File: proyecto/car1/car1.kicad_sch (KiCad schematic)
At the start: 26 parts, among them J1 HC-sr04, J10 vcc Edu ciaa, J11 Adafruit A, J12 Adafruit B, J2 HC-sr04, J3 HC-sr04, J4 usb c socket, J5 SERVO, J6 Conn_01x08_Socket, J7 Conn_01x08_Socket, J8 Conn_01x19, J9 Conn_01x19

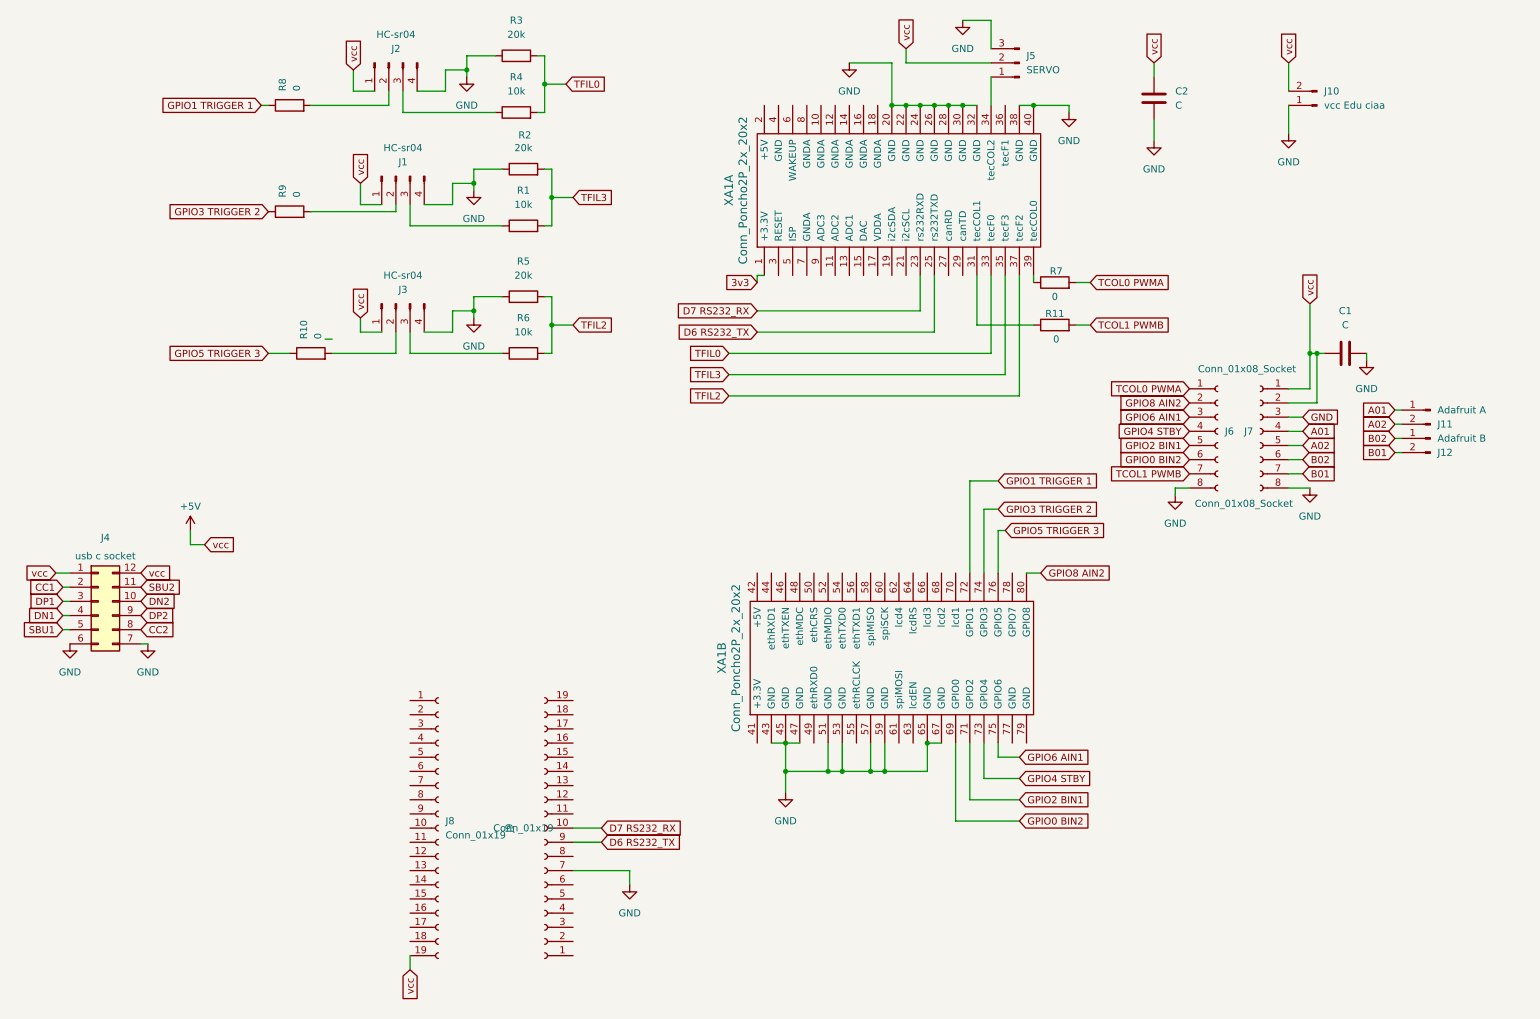
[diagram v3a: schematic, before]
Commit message: cambio de pines
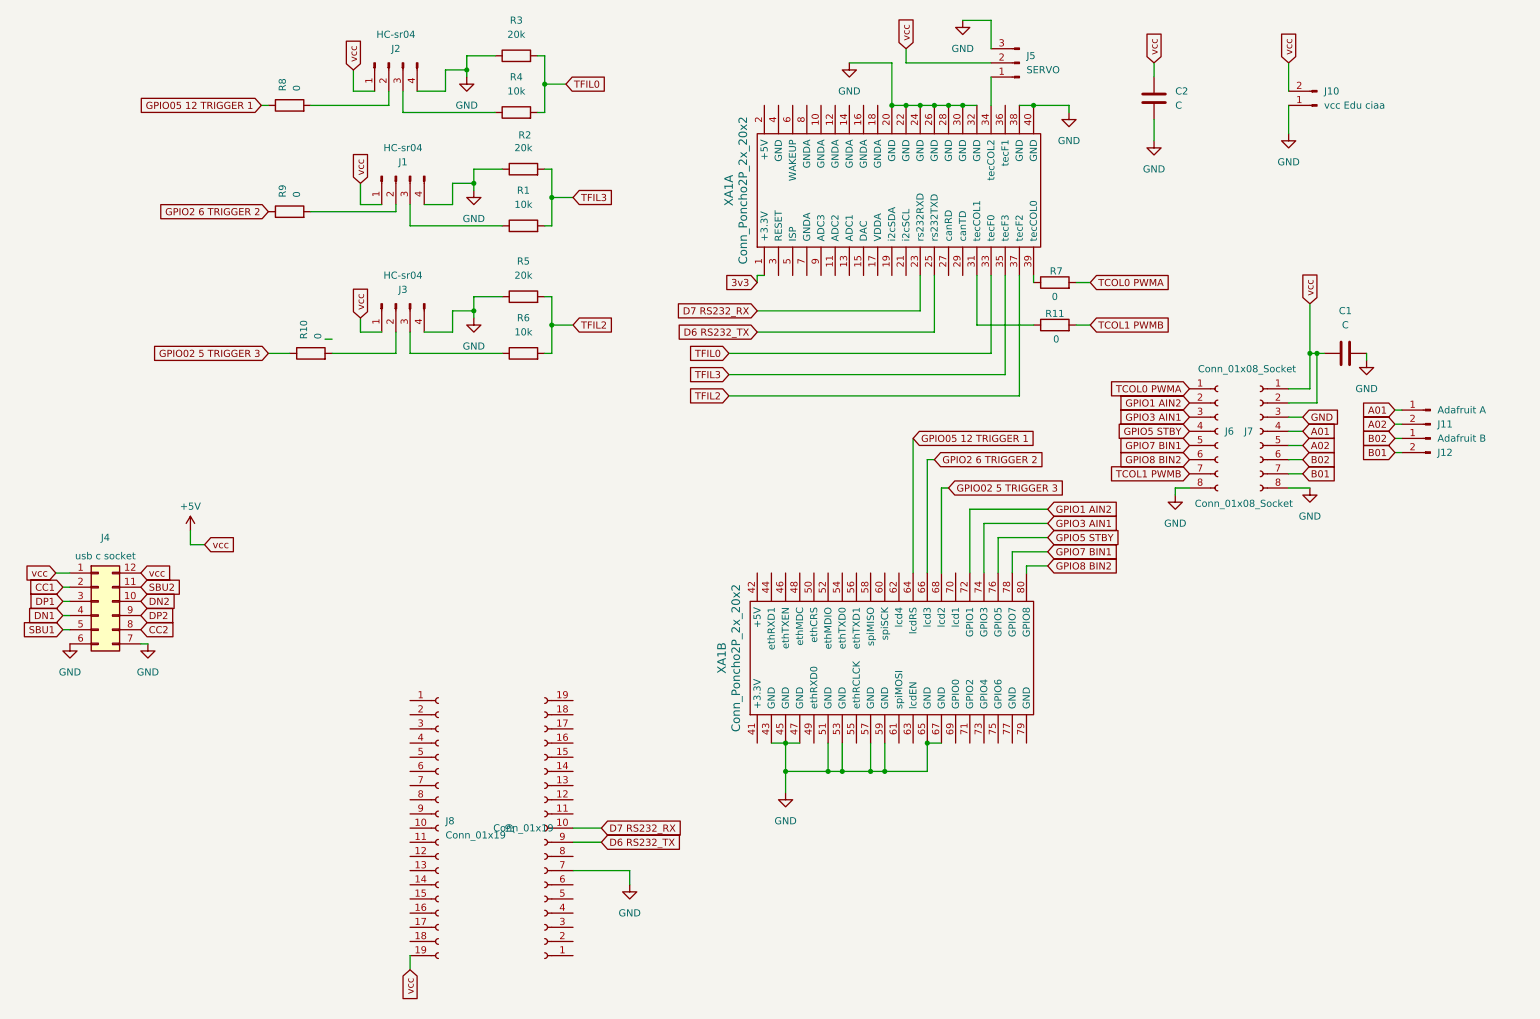
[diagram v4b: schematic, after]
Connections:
- net GPIO05 12 TRIGGER 1: now reaches XA1.64 (lcdRS)
- net GPIO05 12 TRIGGER 1: now also R8.1
- net GPIO2 6  TRIGGER 2: now reaches XA1.66 (lcd3)
- net GPIO2 6  TRIGGER 2: now also R9.1
- net GPIO02 5 TRIGGER 3: now reaches XA1.68 (lcd2)
- net GPIO02 5 TRIGGER 3: now also R10.1
- net GPIO7 BIN1: now reaches XA1.78 (GPIO7)
- net GPIO7 BIN1: now also J6.5 (Pin_5)
- net GPIO0 BIN2: no longer names the net of XA1.69 (GPIO0)
- net GPIO0 BIN2: no longer J6.6 (Pin_6)
- net GPIO1 TRIGGER 1 renamed GPIO1 AIN2
- net GPIO1 AIN2: now also J6.2 (Pin_2); no longer R8.1
- net GPIO2 BIN1: no longer names the net of XA1.71 (GPIO2)
- net GPIO2 BIN1: no longer J6.5 (Pin_5)
- net GPIO3  TRIGGER 2 renamed GPIO3 AIN1
- net GPIO3 AIN1: now also J6.3 (Pin_3); no longer R9.1
- net GPIO4 STBY: no longer names the net of XA1.73 (GPIO4)
- net GPIO4 STBY: no longer J6.4 (Pin_4)
- net GPIO5 TRIGGER 3 renamed GPIO5 STBY
- net GPIO5 STBY: now also J6.4 (Pin_4); no longer R10.1
- net GPIO6 AIN1: no longer names the net of XA1.75 (GPIO6)
- net GPIO6 AIN1: no longer J6.3 (Pin_3)
- net GPIO8 AIN2 renamed GPIO8 BIN2
- net GPIO8 BIN2: now also J6.6 (Pin_6); no longer J6.2 (Pin_2)

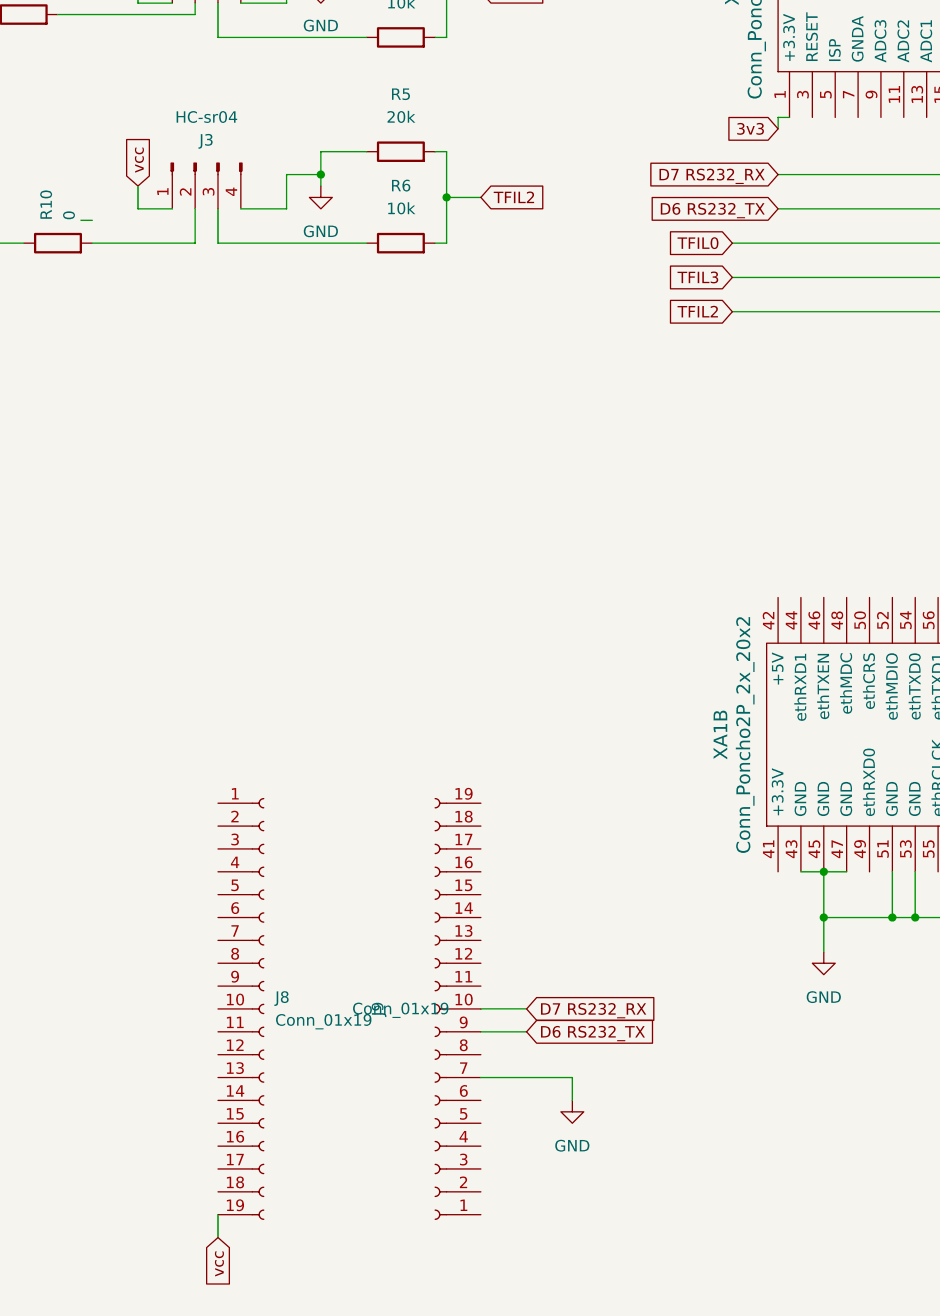
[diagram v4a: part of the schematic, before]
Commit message: fix esp32
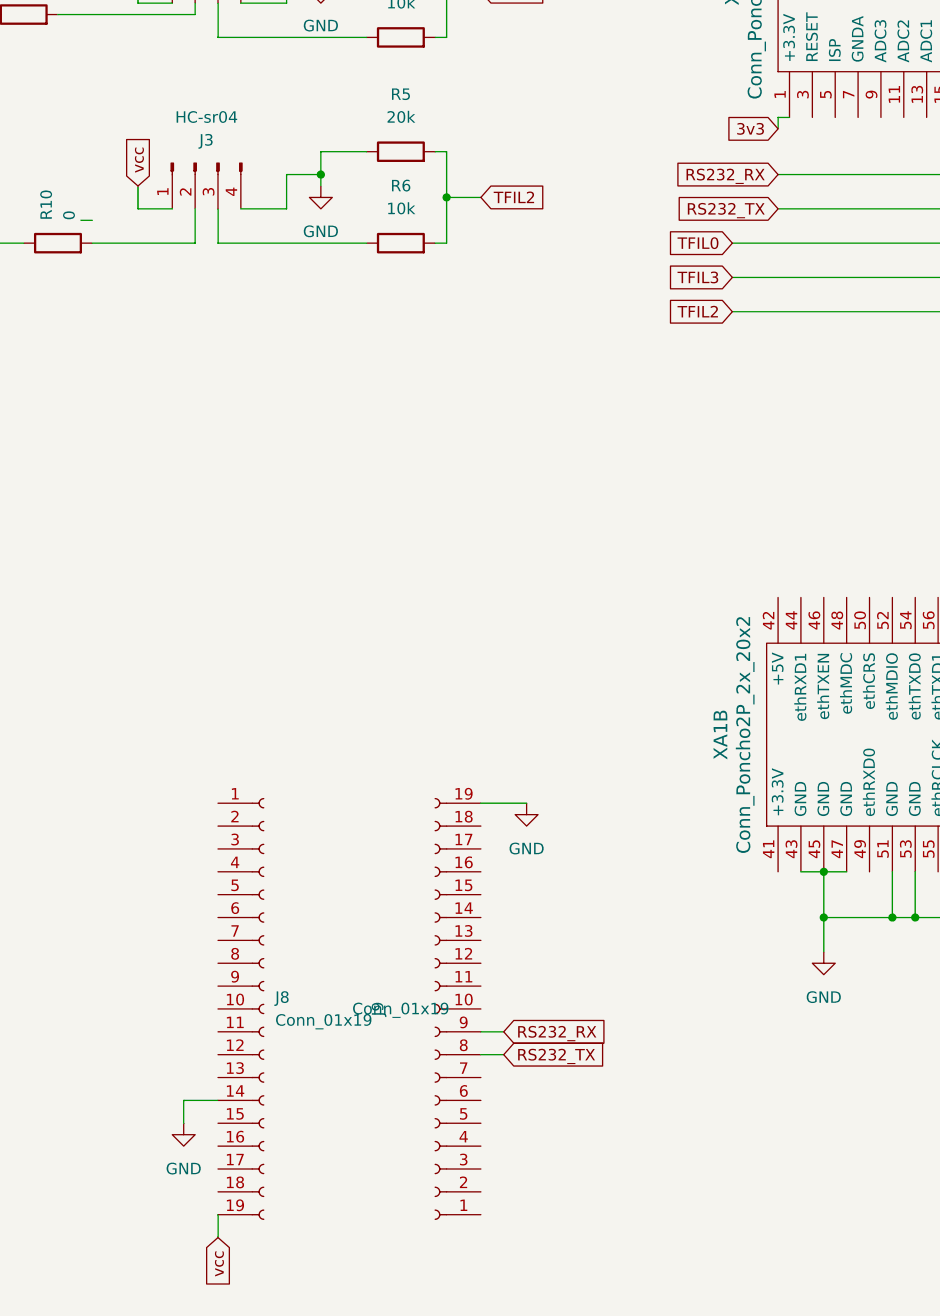
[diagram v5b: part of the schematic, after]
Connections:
- net GND: now also J8.14 (Pin_14), J9.19 (Pin_19); no longer J9.7 (Pin_7)
- net RS232_TX: now reaches J9.8 (Pin_8)
- net RS232_TX: now also XA1.25 (rs232TXD)
- net D6  RS232_TX renamed RS232_RX
- net RS232_RX: now also XA1.23 (rs232RXD); no longer XA1.25 (rs232TXD)
- net D7  RS232_RX: no longer names the net of J9.10 (Pin_10)
- net D7  RS232_RX: no longer XA1.23 (rs232RXD)
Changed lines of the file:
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@@
 	(wire
 		(pts
-			(xy 129.54 167.64) (xy 129.54 170.18)
-		)
-		(stroke
-			(width 0)
-			(type default)
-		)
-	)
-	(wire
-		(pts
 			(xy 254 74.93) (xy 252.73 74.93)
 		)
@@
 	(wire
 		(pts
-			(xy 119.38 167.64) (xy 129.54 167.64)
-		)
-		(stroke
-			(width 0)
-			(type default)
-		)
-	)
-	(wire
-		(pts
 			(xy 247.65 30.48) (xy 247.65 35.56)
 		)
@@
 	(wire
 		(pts
-			(xy 124.46 162.56) (xy 119.38 162.56)
+			(xy 27.94 124.46) (xy 29.21 124.46)
 		)
 		(stroke
@@
 	(wire
 		(pts
-			(xy 27.94 124.46) (xy 29.21 124.46)
+			(xy 119.38 162.56) (xy 121.92 162.56)
 		)
 		(stroke
@@
 	(wire
 		(pts
+			(xy 119.38 165.1) (xy 121.92 165.1)
+		)
+		(stroke
+			(width 0)
+			(type default)
+		)
+	)
+	(wire
+		(pts
 			(xy 86.36 30.48) (xy 86.36 27.94)
 		)
@@
 	(wire
 		(pts
+			(xy 86.36 170.18) (xy 86.36 172.72)
+		)
+		(stroke
+			(width 0)
+			(type default)
+		)
+	)
+	(wire
+		(pts
 			(xy 27.94 116.84) (xy 29.21 116.84)
 		)
@@
 	(wire
 		(pts
-			(xy 124.46 160.02) (xy 119.38 160.02)
-		)
-		(stroke
-			(width 0)
-			(type default)
-		)
-	)
-	(wire
-		(pts
 			(xy 157.48 149.86) (xy 157.48 153.67)
 		)
@@
 	(wire
 		(pts
+			(xy 119.38 137.16) (xy 124.46 137.16)
+		)
+		(stroke
+			(width 0)
+			(type default)
+		)
+	)
+	(wire
+		(pts
 			(xy 154.94 144.78) (xy 157.48 144.78)
 		)
@@
 	(wire
 		(pts
+			(xy 86.36 170.18) (xy 90.17 170.18)
+		)
+		(stroke
+			(width 0)
+			(type default)
+		)
+	)
+	(wire
+		(pts
 			(xy 115.57 41.91) (xy 115.57 46.99)
 		)
@@
 		)
 	)
+	(global_label "RS232_RX"
+		(shape input)
+		(at 121.92 162.56 0)
+		(fields_autoplaced yes)
+		(effects
+			(font
+				(size 1.27 1.27)
+			)
+			(justify left)
+		)
+		(property "Intersheetrefs" "${INTERSHEET_REFS}"
+			(at 134.4603 162.56 0)
+			(effects
+				(font
+					(size 1.27 1.27)
+				)
+				(justify left)
+				(hide yes)
+			)
+		)
+	)
 	(global_label "GPIO5 STBY"
 		(shape input)
@@
 		)
 	)
-	(global_label "D7  RS232_RX"
-		(shape input)
-		(at 124.46 160.02 0)
-		(fields_autoplaced yes)
-		(effects
-			(font
-				(size 1.27 1.27)
-			)
-			(justify left)
-		)
-		(property "Intersheetrefs" "${INTERSHEET_REFS}"
-			(at 141.415 160.02 0)
-			(effects
-				(font
-					(size 1.27 1.27)
-				)
-				(justify left)
-				(hide yes)
-			)
-		)
-	)
 	(global_label "GPIO1 AIN2"
 		(shape input)
@@
 		)
 	)
-	(global_label "D6  RS232_TX"
+	(global_label "RS232_TX"
 		(shape input)
 		(at 152.4 71.12 180)
@@
 		)
 		(property "Intersheetrefs" "${INTERSHEET_REFS}"
-			(at 135.7474 71.12 0)
+			(at 140.1621 71.12 0)
 			(effects
 				(font
@@
 		)
 	)
-	(global_label "D7  RS232_RX"
+	(global_label "RS232_RX"
 		(shape input)
 		(at 152.4 67.31 180)
@@
 		)
 		(property "Intersheetrefs" "${INTERSHEET_REFS}"
-			(at 135.445 67.31 0)
+			(at 139.8597 67.31 0)
 			(effects
 				(font
@@
 		)
 	)
-	(global_label "D6  RS232_TX"
+	(global_label "RS232_TX"
 		(shape input)
-		(at 124.46 162.56 0)
+		(at 121.92 165.1 0)
 		(fields_autoplaced yes)
 		(effects
@@
 		)
 		(property "Intersheetrefs" "${INTERSHEET_REFS}"
-			(at 141.1126 162.56 0)
+			(at 134.1579 165.1 0)
 			(effects
 				(font
@@
 	(symbol
 		(lib_id "power:GND")
-		(at 129.54 170.18 0)
+		(at 86.36 172.72 0)
 		(unit 1)
 		(exclude_from_sim no)
@@
 		(fields_autoplaced yes)
 		(property "Reference" "#PWR03"
-			(at 129.54 176.53 0)
+			(at 86.36 179.07 0)
 			(effects
 				(font
@@
 		)
 		(property "Value" "GND"
-			(at 129.54 175.26 0)
+			(at 86.36 177.8 0)
 			(effects
 				(font
@@
 		)
 		(property "Footprint" ""
-			(at 129.54 170.18 0)
+			(at 86.36 172.72 0)
 			(effects
 				(font
@@
 		)
 		(property "Datasheet" ""
-			(at 129.54 170.18 0)
+			(at 86.36 172.72 0)
 			(effects
 				(font
@@
 		)
 		(property "Description" "Power symbol creates a global label with name \"GND\" , ground"
-			(at 129.54 170.18 0)
+			(at 86.36 172.72 0)
 			(effects
 				(font
@@
 		)
 		(instances
-			(project ""
+			(project "car1"
 				(path "/be9e834b-7dff-4f8a-8442-6085dd680417"
 					(reference "#PWR03")
@@
 					(unit 1)
 				)
+			)
+		)
+	)
+	(symbol
+		(lib_id "power:GND")
+		(at 124.46 137.16 0)
+		(unit 1)
+		(exclude_from_sim no)
+		(in_bom yes)
+		(on_board yes)
+		(dnp no)
+		(fields_autoplaced yes)
+		(property "Reference" "#PWR014"
+			(at 124.46 143.51 0)
+			(effects
+				(font
+					(size 1.27 1.27)
+				)
+				(hide yes)
+			)
+		)
+		(property "Value" "GND"
+			(at 124.46 142.24 0)
+			(effects
+				(font
+					(size 1.27 1.27)
+				)
+			)
+		)
+		(property "Footprint" ""
+			(at 124.46 137.16 0)
+			(effects
+				(font
+					(size 1.27 1.27)
+				)
+				(hide yes)
+			)
+		)
+		(property "Datasheet" ""
+			(at 124.46 137.16 0)
+			(effects
+				(font
+					(size 1.27 1.27)
+				)
+				(hide yes)
+			)
+		)
+		(property "Description" "Power symbol creates a global label with name \"GND\" , ground"
+			(at 124.46 137.16 0)
+			(effects
+				(font
+					(size 1.27 1.27)
+				)
+				(hide yes)
+			)
+		)
+		(pin "1"
+		)
+		(instances
+			(project "car1"
+				(path "/be9e834b-7dff-4f8a-8442-6085dd680417"
+					(reference "#PWR014")
+					(unit 1)
+				)
